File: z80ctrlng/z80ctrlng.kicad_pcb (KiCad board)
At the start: 2 copper layers, 99.8 x 49.9 mm, 54 parts, among them J1 BUS, J10 QWIIC, J11 CLOCK, J2 MICRO_SD, J3 UEXT, J4 SERIAL, J5 3V_LINK, J6 UPDI, J7 UEXT_CS, J8 S1_LINK, J9 S2_LINK, Q1 BSS138, SW1 RESET, SW2 BANK_EN, SW3 RTC, SW4 RTC, U1 AVR128DB64x-xPT, U2 MIC5504-3.3YM5, U3 MCP7940N-xST, U5 74HCT574, U6 74HCT257, U7 AS6C4008-55PCN, Y1 32kHz

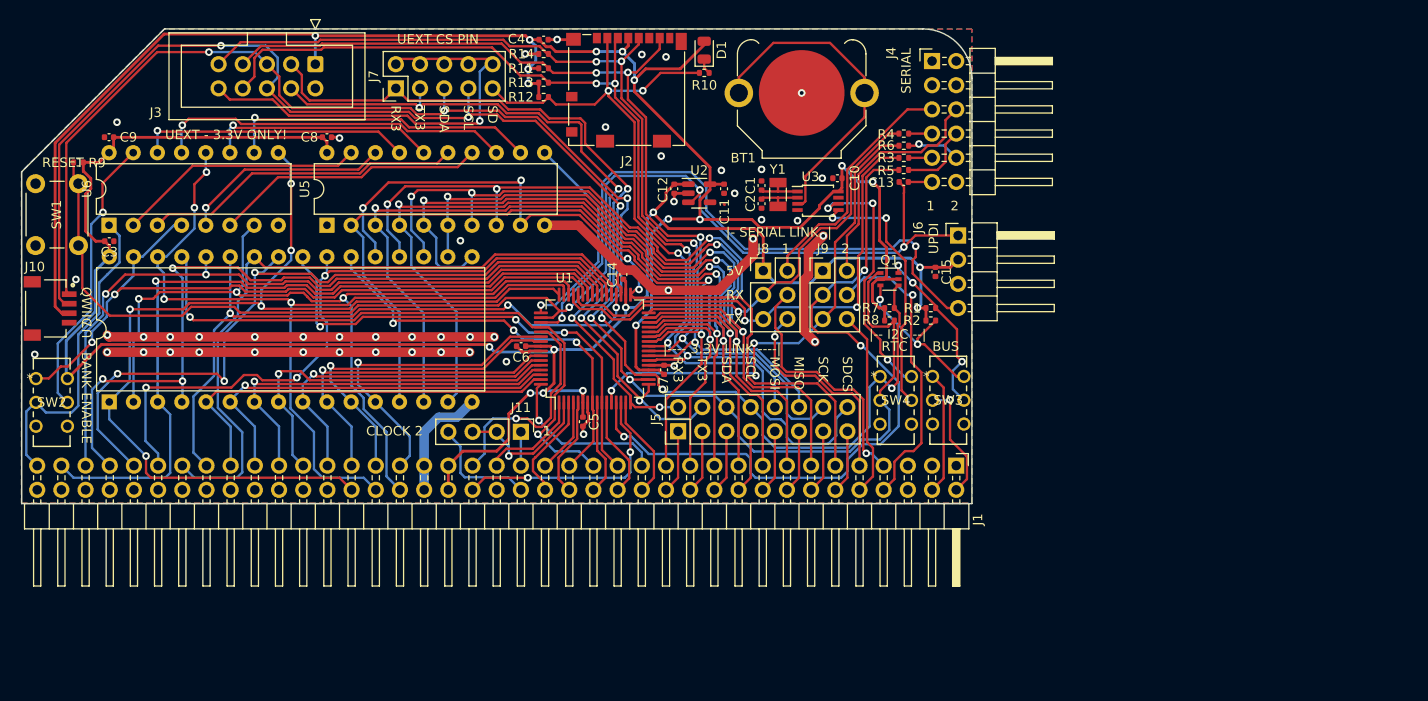
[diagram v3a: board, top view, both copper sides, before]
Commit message: Switch to RCBus-80 footprints, JLCPCB preferred components
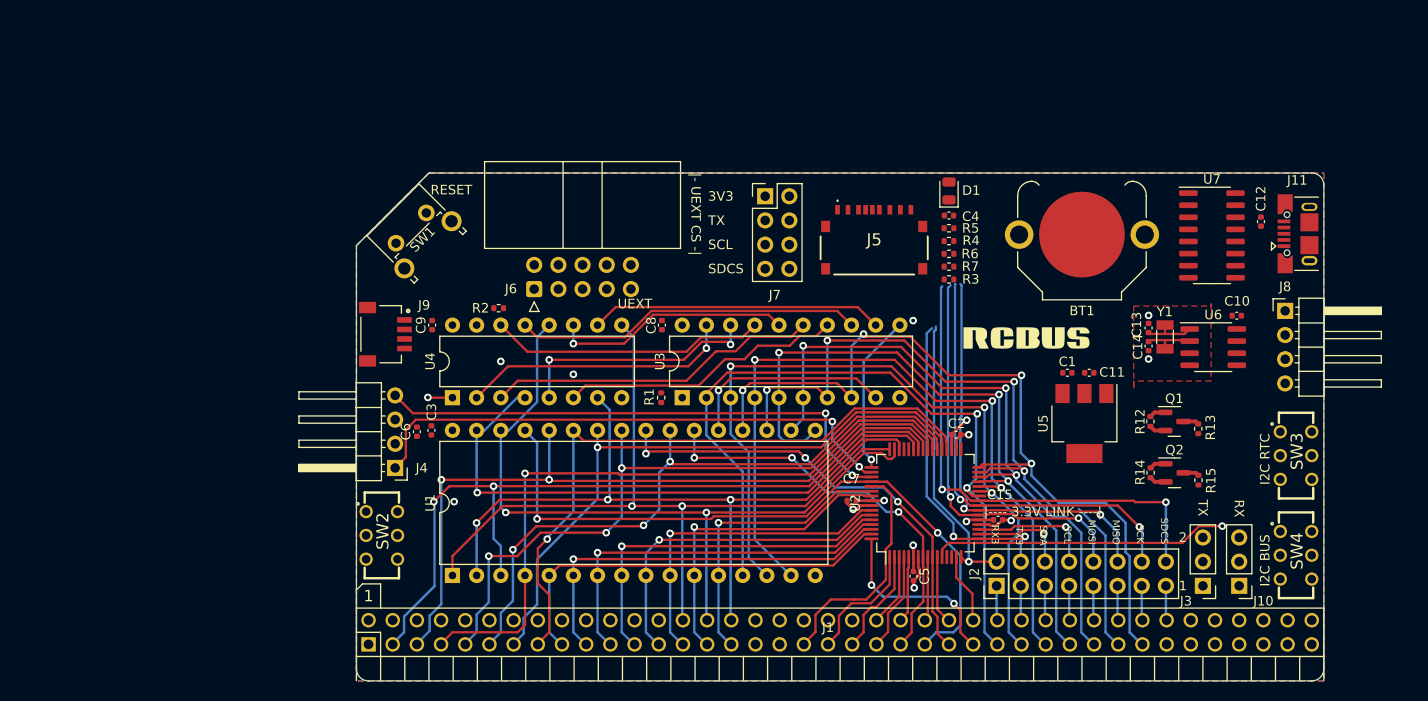
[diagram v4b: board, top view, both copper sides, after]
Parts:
- removed R10: 330, Resistor_SMD:R_0402_1005Metric
- removed R11: 100K, Resistor_SMD:R_0402_1005Metric
- removed R8: 4.7K, Resistor_SMD:R_0402_1005Metric
- removed R9: 1K, Resistor_SMD:R_0402_1005Metric
- added LOGO3: RCBUS_Logo, My_Components:RCBUS_Logo, F.Cu at (198.4, 90.7)
- added Q2: BSS138, Package_TO_SOT_SMD:SOT-23, F.Cu at (213.7, 104.9)
- added R15: 4.7K, Resistor_SMD:R_0402_1005Metric, F.Cu at (216.2, 105.7)
- added U4: 74HCT257, Package_DIP:DIP-16_W7.62mm, F.Cu at (137.8, 97.0)
- BT1: value Battery -> CR1216
- C1, C2: value 0.6pf -> 0.1uf
- C10, C9: value 0.1uf -> 1uf
- C11, C12: value 1uf -> 0.1uf
- C13, C14: value 0.1uf -> 0.6pf
- J1: value BUS -> RCBus-80; footprint Connector_PinHeader_2.54mm:PinHeader_2x39_P2.54mm_Horizontal -> Custom:RCBus-80
- J10: value QWIIC -> RX_LINK; footprint Custom:JST_SM04B-SRSS-TB_LF__SN_ -> Connector_PinHeader_2.54mm:PinHeader_1x03_P2.54mm_Vertical
- J11: value CLOCK -> USB_B_Micro; footprint Connector_PinHeader_2.54mm:PinHeader_1x04_P2.54mm_Vertical -> Connector_USB:USB_Micro-B_XKB_U254-051T-4BH83-F1S
- J2: value MICRO_SD -> 3V_LINK; footprint Connector_Card:microSD_HC_Molex_104031-0811 -> Connector_PinHeader_2.54mm:PinHeader_2x08_P2.54mm_Vertical
- J3: value UEXT -> TX_LINK; footprint Connector_IDC:IDC-Header_2x05_P2.54mm_Vertical -> Connector_PinHeader_2.54mm:PinHeader_1x03_P2.54mm_Vertical
- J4: value SERIAL -> UPDI; footprint Connector_PinHeader_2.54mm:PinHeader_2x06_P2.54mm_Horizontal -> Connector_PinHeader_2.54mm:PinHeader_1x04_P2.54mm_Horizontal
- J5: value 3V_LINK -> XKTF-0803-0; footprint Connector_PinHeader_2.54mm:PinHeader_2x08_P2.54mm_Vertical -> SamacSys_Parts:XKTF08030
- J6: value UPDI -> UEXT; footprint Connector_PinHeader_2.54mm:PinHeader_1x04_P2.54mm_Horizontal -> Connector_IDC:IDC-Header_2x05_P2.54mm_Horizontal
- J7: value UEXT_CS -> UXCS; footprint Connector_PinHeader_2.54mm:PinHeader_2x05_P2.54mm_Vertical -> Connector_PinHeader_2.54mm:PinHeader_2x04_P2.54mm_Vertical
- J8: value S1_LINK -> SERIAL; footprint Connector_PinHeader_2.54mm:PinHeader_2x03_P2.54mm_Vertical -> Connector_PinHeader_2.54mm:PinHeader_1x04_P2.54mm_Horizontal
- J9: value S2_LINK -> SM04B-SRSS-TB; footprint Connector_PinHeader_2.54mm:PinHeader_2x03_P2.54mm_Vertical -> Custom:JST_SM04B-SRSS-TB_LF__SN_
- Q1: footprint Package_TO_SOT_SMD:SOT-363_SC-70-6 -> Package_TO_SOT_SMD:SOT-23
- R1, R2: value 4.7K -> 10K
- R12, R13, R14: value 100K -> 4.7K
- R3, R4, R6: value 1K -> 100K
- R5: value 1K -> 100
- R7: value 4.7K -> 100K
- SW1: footprint Button_Switch_THT:SW_PUSH_6mm -> Button_Switch_THT:SW_Tactile_SPST_Angled_PTS645Vx31-2LFS
- SW2, SW3: footprint Custom:SWITCH_011CQN -> SamacSys_Parts:JS202011CQN
- SW4: value RTC -> BUS; footprint Custom:SWITCH_011CQN -> SamacSys_Parts:JS202011CQN
- U1: value AVR128DB64x-xPT -> AS6C4008-55PCN; footprint Package_QFP:TQFP-64_10x10mm_P0.5mm -> Package_DIP:DIP-32_W15.24mm
- U2: value MIC5504-3.3YM5 -> AVR128DB64T-I/PT; footprint Package_TO_SOT_SMD:SOT-23-5 -> Package_QFP:TQFP-64_10x10mm_P0.5mm
- U3: value MCP7940N-xST -> 74HCT574; footprint Package_SO:TSSOP-8_3x3mm_P0.65mm -> Package_DIP:DIP-20_W7.62mm
- U5: value 74HCT574 -> AMS1117-3.3; footprint Package_DIP:DIP-20_W7.62mm -> Package_TO_SOT_SMD:SOT-223-3_TabPin2
- U6: value 74HCT257 -> PCF8563T; footprint Package_DIP:DIP-16_W7.62mm -> Package_SO:SOIC-8_3.9x4.9mm_P1.27mm
- U7: value AS6C4008-55PCN -> CH340C; footprint Package_DIP:DIP-32_W15.24mm -> Package_SO:SOIC-16_3.9x9.9mm_P1.27mm
- moved J10 126.3 mm to (220.5, 116.8), turned to 180 degrees
- moved U7 117.1 mm to (217.6, 80.0), turned to 0 degrees
- moved U6 116.7 mm to (217.7, 91.7), turned to 0 degrees
- moved J3 108.1 mm to (216.7, 116.8), turned to 180 degrees
- moved J11 85.0 mm to (227.5, 79.8), turned to 90 degrees
- moved U5 82.2 mm to (204.2, 99.7), turned to -90 degrees
- moved R13 77.8 mm to (216.2, 100.3), turned to 90 degrees
- moved R14 77.5 mm to (211.2, 104.9), turned to -90 degrees
- moved R12 72.3 mm to (211.1, 99.5), turned to -90 degrees
- moved J4 70.8 mm to (131.8, 104.4), turned to 180 degrees
- moved J2 65.0 mm to (195.0, 116.8), turned to 90 degrees
- moved C12 61.7 mm to (222.8, 78.5), turned to 90 degrees
- moved C14 55.7 mm to (211.0, 91.6), turned to -90 degrees
- moved J8 55.0 mm to (225.3, 87.9)
- moved SW4 47.5 mm to (226.4, 113.6), turned to -90 degrees
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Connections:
- BT1 pad 1: Net-(BT1-+) -> +3.3V
- C1 pad 1: Net-(U3-X1) -> +5V
- C12 pad 1: +5V -> Net-(U7-~{DTR})
- C12 pad 2: GND -> ~{RESET}
- C13 pad 1: Net-(J4-Pin_11) -> Net-(U6-OSCI)
- C13 pad 2: /~{RESET} -> GND
- C14 pad 1: +5V -> Net-(U6-OSCO)
- C15 pad 1: +5V -> +3.3V
- C2 pad 1: Net-(U3-X2) -> +5V
- C7 pad 1: +3.3V -> +5V
- J1 pad 1: /USER3 -> /A15
- J1 pad 10: /BTX2 -> /A6
- J1 pad 11: /D7 -> /A5
- J1 pad 12: /D15 -> /A4
- J1 pad 13: /D6 -> /A3
- J1 pad 14: /D14 -> /A2
- J1 pad 15: /D5 -> /A1
- J1 pad 16: /D13 -> /A0
- J1 pad 17: /D4 -> GND
- J1 pad 18: /D12 -> +5V
- J1 pad 19: /D3 -> /~{M1}
- J1 pad 2: /USER7 -> /A14
- J1 pad 20: /D11 -> /~{Z80RST}
- J1 pad 21: /D2 -> /Z80CLK
- J1 pad 22: /D10 -> /~{INT}
- J1 pad 23: /D1 -> /~{MREQ}
- J1 pad 24: /D9 -> /~{WR}
- J1 pad 25: /D0 -> /~{RD}
- J1 pad 26: /D8 -> /~{IORQ}
- J1 pad 27: /~{IORQ} -> /D0
- J1 pad 28: /~{NMI} -> /D1
- J1 pad 29: /~{RD} -> /D2
- J1 pad 3: /USER2 -> /A13
- J1 pad 30: /~{WAIT} -> /D3
- J1 pad 31: /~{WR} -> /D4
- J1 pad 32: /~{BUSRQ} -> /D5
- J1 pad 33: /~{MREQ} -> /D6
- J1 pad 34: /~{HALT} -> /D7
- J1 pad 35: /~{INT} -> /BTX1
- J1 pad 36: /~{BUSACK} -> /BRX1
- J1 pad 37: /CLOCK1 -> /USER1
- J1 pad 38: /CLOCK2 -> /USER2
- J1 pad 39: /~{Z80RST} -> /USER3
- J1 pad 4: /USER6 -> /A12
- J1 pad 40: /PAGE -> unconnected-(J1-Pin_40-Pad40)
- J1 pad 41: /~{M1} -> /p41
- J1 pad 42: /~{RFSH} -> /p42
- J1 pad 43: +5V -> /p43
- J1 pad 44: +5V -> /p44
- J1 pad 45: GND -> /p45
- J1 pad 46: GND -> /p46
- J1 pad 47: /A0 -> /p47
- J1 pad 48: /A16 -> /p48
- J1 pad 49: /A1 -> /A23
- J1 pad 5: /USER1 -> /A11
- J1 pad 50: /A17 -> /A22
- J1 pad 51: /A2 -> /A21
- J1 pad 52: /A18 -> /A20
- J1 pad 53: /A3 -> /A19
- J1 pad 54: /A19 -> /A18
- J1 pad 55: /A4 -> /A17
- J1 pad 56: /A20 -> /A16
- J1 pad 57: /A5 -> GND
- J1 pad 58: /A21 -> +5V
- J1 pad 59: /A6 -> /~{RFSH}
- J1 pad 6: /USER5 -> /A10
- J1 pad 60: /A22 -> /PAGE
- J1 pad 61: /A7 -> /CLOCK2
- J1 pad 62: /A23 -> /~{BUSACK}
- J1 pad 63: /A8 -> /~{HALT}
- J1 pad 64: /p48 -> /~{BUSRQ}
- J1 pad 65: /A9 -> /~{WAIT}
- J1 pad 66: /p47 -> /~{NMI}
- J1 pad 67: /A10 -> /D8
- J1 pad 68: /p46 -> /D9
- J1 pad 69: /A11 -> /D10
- J1 pad 7: /BRX -> /A9
- J1 pad 70: /p45 -> /D11
- J1 pad 71: /A12 -> /D12
- J1 pad 72: /p44 -> /D13
- J1 pad 73: /A13 -> /D14
- J1 pad 74: /p43 -> /D15
- J1 pad 75: /A14 -> /BTX2
- J1 pad 76: /p42 -> /BRX2
- J1 pad 77: /A15B -> /USER5
- J1 pad 78: /p41 -> SCL5V
- J1 pad 8: /BRX2 -> /A8
- J1 pad 9: /BTX -> /A7
- J10 pad 1: /SCL -> /BRX1
- J10 pad 2: /SDA -> RX2
- J10 pad 3: +3.3V -> /BRX2
- J11 pad 1: /CLOCK1 -> unconnected-(J11-VBUS-Pad1)
- J11 pad 2: /Z80CLK -> unconnected-(J11-D--Pad2)
- J11 pad 3: /Z80CLK -> unconnected-(J11-D+-Pad3)
- J11 pad 4: /CLOCK2 -> unconnected-(J11-ID-Pad4)
- J2 pad 1: unconnected-(J2-DAT2-Pad1) -> /D8
- J2 pad 10: unconnected-(J2-DET_A-Pad10) -> MOSI
- J2 pad 11: GND -> /D13
- J2 pad 2: /~{SDCS} -> RX3
- J2 pad 3: /MOSI -> /D9
- J2 pad 4: +3.3V -> TX3
- J2 pad 5: /SCK -> /D10
- J2 pad 6: GND -> SDA
- J2 pad 7: /MISO -> /D11
- J2 pad 8: unconnected-(J2-DAT1-Pad8) -> SCL
- J2 pad 9: unconnected-(J2-DET_B-Pad9) -> /D12
- J3 pad 1: +3.3V -> /BTX1
- J3 pad 2: GND -> TX2
- J3 pad 3: /TX3 -> /BTX2
- J4 pad 1: GND -> ~{RESET}
- J4 pad 2: GND -> +5V
- J4 pad 3: unconnected-(J4-Pin_3-Pad3) -> GND
- J4 pad 4: unconnected-(J4-Pin_4-Pad4) -> UPDI
- J6 pad 1: /~{RESET} -> +3.3V
- J6 pad 2: +5V -> GND
- J6 pad 3: GND -> TX3
- J6 pad 4: /UPDI -> RX3
- J7 pad 1: /TX3 -> +3.3V
- J7 pad 2: /~{UXCS} -> Net-(J6-Pin_10)
- J7 pad 3: /RX3 -> TX3
- J7 pad 4: /~{UXCS} -> Net-(J6-Pin_10)
- J7 pad 5: /SCL -> SCL
- J7 pad 6: /~{UXCS} -> Net-(J6-Pin_10)
- J7 pad 7: /SDA -> ~{SDCS}
- J7 pad 8: /~{UXCS} -> Net-(J6-Pin_10)
- J8 pad 2: /5VS1 -> RX2
- J8 pad 3: /RX -> TX2
- J8 pad 4: /BRX -> GND
- J9 pad 1: +5V -> SCL
- J9 pad 2: /5VS2 -> SDA
- J9 pad 3: /RX2 -> +3.3V
- J9 pad 4: /BRX2 -> GND
- Q1 pad 1: /SDA -> +3.3V
- Q1 pad 2: +3.3V -> Net-(Q1-S)
- Q1 pad 3: /SCL5V -> Net-(Q1-D)
- R1 pad 1: +5V -> /~{MREQ}
- R1 pad 2: /SDA5V -> +5V
- R12 pad 2: /~{SDCS} -> Net-(Q1-S)
- R13 pad 1: +3.3V -> +5V
- R13 pad 2: /MOSI -> Net-(Q1-D)
- R14 pad 1: GND -> +3.3V
- R14 pad 2: /SCK -> Net-(Q2-S)
- R2 pad 1: +5V -> ~{RESET}
- R2 pad 2: /SCL5V -> +5V
- R3 pad 1: Net-(J4-Pin_9) -> Net-(R3-Pad1)
- R3 pad 2: /TX -> MISO
- R4 pad 1: Net-(J4-Pin_7) -> Net-(R3-Pad1)
- R4 pad 2: /RX -> ~{SDCS}
- R5 pad 1: /RX2 -> ~{SDCS}
- R5 pad 2: Net-(J4-Pin_8) -> Net-(D1-K)
- R6 pad 1: Net-(J4-Pin_10) -> Net-(R3-Pad1)
- R6 pad 2: /TX2 -> MOSI
- R7 pad 1: +3.3V -> GND
- R7 pad 2: /SCL -> SCK
- SW1 pad 2: /~{RESET} -> ~{RESET}
- SW2 pad 2: /A15B -> /A15
- SW3 pad 1: /USER6 -> Net-(Q2-S)
- SW3 pad 2: /USER7 -> SDA
- SW3 pad 4: unconnected-(SW3-Pad4) -> Net-(Q1-S)
- SW3 pad 5: /SDA5V -> SCL
- SW3 pad 6: /SCL5V -> unconnected-(SW3-Pad6)
- SW4 pad 1: /SCL -> Net-(Q2-D)
- SW4 pad 2: /SDA -> SCL5V
- SW4 pad 4: unconnected-(SW4-Pad4) -> Net-(Q1-D)
- SW4 pad 5: Net-(U3-SDA) -> SDA5V
- SW4 pad 6: Net-(U3-SCL) -> unconnected-(SW4-Pad6)
- U1 pad 1: /~{Z80RST} -> /A18
- U1 pad 10: /~{RD} -> /A2
- U1 pad 11: /~{WAIT} -> /A1
- U1 pad 12: /TX2 -> /A0
- U1 pad 13: /RX2 -> /D0
- U1 pad 14: /~{RFSH} -> /D1
- U1 pad 15: /~{NMI} -> /D2
- U1 pad 16: /RX3 -> GND
- U1 pad 17: /TX3 -> /D3
- U1 pad 18: /SDA -> /D4
- U1 pad 19: /SCL -> /D5
- U1 pad 2: /Z80CLK -> /A16
- U1 pad 20: +3.3V -> /D6
- U1 pad 21: GND -> /D7
- U1 pad 22: /MOSI -> /~{MREQ}
- U1 pad 23: /MISO -> /A10
- U1 pad 24: /SCK -> /~{RD}
- U1 pad 25: /~{SDCS} -> /A11
- U1 pad 26: /D0 -> /A9
- U1 pad 27: /D1 -> /A8
- U1 pad 28: /D2 -> /A13
- U1 pad 29: /D3 -> /~{WR}
- U1 pad 3: /~{BUSACK} -> /A14
- U1 pad 30: /D4 -> /A17
- U1 pad 31: /D5 -> /A15
- U1 pad 32: /D6 -> +5V
- U1 pad 4: /~{INT} -> /A12
- U1 pad 5: /~{HALT} -> /A7
- U1 pad 6: +5V -> /A6
- U1 pad 7: GND -> /A5
- U1 pad 8: /~{MREQ} -> /A4
- U1 pad 9: /~{BUSRQ} -> /A3
- U2 pad 1: +5V -> /~{Z80RST}
- U2 pad 2: GND -> /Z80CLK
- U2 pad 3: /~{RESET} -> /~{BUSACK}
- U2 pad 4: unconnected-(U2-NC-Pad4) -> /~{INT}
- U2 pad 5: +3.3V -> /~{HALT}
- U3 pad 1: Net-(U3-X1) -> GND
- U3 pad 2: Net-(U3-X2) -> /D0
- U3 pad 3: Net-(BT1-+) -> /D1
- U3 pad 4: GND -> /D2
- U3 pad 5: Net-(U3-SDA) -> /D3
- U3 pad 6: Net-(U3-SCL) -> /D4
- U3 pad 7: unconnected-(U3-MFP-Pad7) -> /D5
- U3 pad 8: +3.3V -> /D6
- U5 pad 2: /D0 -> +3.3V
- U5 pad 3: /D1 -> +5V
- U6 pad 1: /A15B -> Net-(U6-OSCI)
- U6 pad 2: /BA15 -> Net-(U6-OSCO)
- U6 pad 3: /BB15 -> unconnected-(U6-~{INT}-Pad3)
- U6 pad 4: /A15 -> GND
- U6 pad 5: /BA16 -> Net-(Q1-S)
- U6 pad 6: /BB16 -> Net-(Q2-S)
- U6 pad 7: /A16 -> unconnected-(U6-CLKO-Pad7)
- U6 pad 8: GND -> +3.3V
- U7 pad 1: /A18 -> unconnected-(U7-GND-Pad1)
- U7 pad 10: /A2 -> unconnected-(U7-~{DSR}-Pad10)
- U7 pad 11: /A1 -> unconnected-(U7-~{RI}-Pad11)
- U7 pad 12: /A0 -> unconnected-(U7-~{DCD}-Pad12)
- U7 pad 13: /D0 -> Net-(U7-~{DTR})
- U7 pad 14: /D1 -> unconnected-(U7-~{RTS}-Pad14)
- U7 pad 15: /D2 -> unconnected-(U7-R232-Pad15)
- U7 pad 16: GND -> unconnected-(U7-VCC-Pad16)
- U7 pad 2: /A16 -> unconnected-(U7-TXD-Pad2)
- U7 pad 3: /A14 -> unconnected-(U7-RXD-Pad3)
- U7 pad 4: /A12 -> unconnected-(U7-V3-Pad4)
- U7 pad 5: /A7 -> unconnected-(U7-UD+-Pad5)
- U7 pad 6: /A6 -> unconnected-(U7-UD--Pad6)
- U7 pad 7: /A5 -> unconnected-(U7-NC-Pad7)
- U7 pad 8: /A4 -> unconnected-(U7-NC-Pad8)
- U7 pad 9: /A3 -> unconnected-(U7-~{CTS}-Pad9)
- Y1 pad 1: Net-(U3-X2) -> Net-(U6-OSCO)
- Y1 pad 2: Net-(U3-X1) -> Net-(U6-OSCI)
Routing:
- net +5V: track 218.1 -> 8.29 mm, vias 9 -> 4
- net +3.3V: track 196.8 -> 7.19 mm, vias 12 -> 1
- net /SDA: track 172.2 -> 0.00 mm, vias 5 -> 0
- net /SCL: track 159.9 -> 0.00 mm, vias 6 -> 0
- net GND: track 150.9 -> 13.6 mm, vias 49 -> 8
- net /~{RESET}: track 137.0 -> 0.00 mm, vias 3 -> 0
- net /SCK: track 106.7 -> 0.00 mm, vias 4 -> 0
- net /MISO: track 102.0 -> 0.00 mm, vias 4 -> 0
- net /MOSI: track 99.9 -> 0.00 mm, vias 4 -> 0
- net /~{SDCS}: track 92.5 -> 0.00 mm, vias 4 -> 0
- net /TX3: track 81.2 -> 0.00 mm, vias 3 -> 0
- net /RX2: track 77.5 -> 0.00 mm, vias 3 -> 0
- net /RX3: track 75.7 -> 0.00 mm, vias 4 -> 0
- net /UPDI: track 66.4 -> 0.00 mm, vias 2 -> 0
- net /D7: track 84.4 -> 22.1 mm, vias 4 -> 1
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- added copper zone on F.Cu, net +5V
- added copper zone on In2.Cu, net +5V
- added copper zone on In1.Cu, net GND
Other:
- board size 99.8 x 49.9 mm -> 101.6 x 53.3 mm
- copper layers 2 -> 4
- board text added: "I2C BUS"
- board text added: "I2C RTC"
- board text added: "PA5 PA6"
- board text added: "PA7 PB0"
- board text added: "PB1 PG0"
- board text added: "PB3 PB2"
- board text added: "PB7 PA2"
- board text added: "UEXT"
- board text added: "|- UEXT CS -|"
- board text removed: "BANK ENABLE"
- board text removed: "BUS"
- board text removed: "CLOCK 2"
- board text removed: "PA2"
- board text removed: "PA5^"
- board text removed: "PA6"
- board text removed: "PA7^"
- board text removed: "PB1^"
- board text removed: "PB3^"
- board text removed: "PB4^"
- board text removed: "PB5^"
- board text removed: "PB6^"
- board text removed: "PB7^"
- board text removed: "PF0^"
- board text removed: "PF1^"
- board text removed: "PF2^"
- board text removed: "PF3^"
- board text removed: "PF4^"
- board text removed: "QWIIC"
- board text removed: "RTC"
- board text removed: "SD"
- board text removed: "SERIAL"
- board text removed: "UEXT - 3.3V ONLY!"
- board text removed: "UEXT CS PIN"
- board text removed: "UPDI"
- board text removed: "|- SERIAL LINK -|"
- board text removed: "|-- I2C --|"

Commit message: Final touches... I hope
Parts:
- removed J8: SERIAL, Connector_PinHeader_2.54mm:PinHeader_1x04_P2.54mm_Horizontal
- added C16: 0.1uf, Capacitor_SMD:C_0402_1005Metric, F.Cu at (220.3, 75.3)
- added D2: 1N5819WS, Diode_SMD:D_SOD-323_HandSoldering, F.Cu at (216.5, 88.9)
- added D3: 1N5819WS, Diode_SMD:D_SOD-323_HandSoldering, F.Cu at (211.8, 88.8)
- added H1: MountingHole, MountingHole:MountingHole_3.2mm_M3, F.Cu at (132.8, 91.2)
- added R8: 1K, Resistor_SMD:R_0402_1005Metric, F.Cu at (212.8, 85.8)
- C10, C9: footprint Capacitor_SMD:C_0402_1005Metric -> Capacitor_SMD:C_1206_3216Metric
- J11: value USB_B_Micro -> U254-051T-4BH81-S2S; footprint Connector_USB:USB_Micro-B_XKB_U254-051T-4BH83-F1S -> SamacSys_Parts:U254051T4BH81S2S
- J4: value UPDI -> DEBUG; footprint Connector_PinHeader_2.54mm:PinHeader_1x04_P2.54mm_Horizontal -> Connector_PinHeader_2.54mm:PinHeader_2x04_P2.54mm_Horizontal
- U2: value AVR128DB64T-I/PT -> AVR128DB64x-xPT
- moved J4 95.2 mm to (225.6, 87.6), turned to 0 degrees
- moved C6 89.6 mm to (223.2, 91.5), turned to -90 degrees
- moved C9 68.6 mm to (203.1, 101.9), turned to -90 degrees
- moved C1 64.8 mm to (137.9, 87.8), turned to 180 degrees
- moved C15 31.4 mm to (220.2, 90.9)
- moved C11 20.3 mm to (193.0, 111.0), turned to 90 degrees
- moved C10 15.3 mm to (212.9, 101.9), turned to 90 degrees
- moved J9 10.4 mm to (132.8, 100.8)
- moved C12 9.14 mm to (223.2, 87.6), turned to -90 degrees
- moved C4 8.24 mm to (182.2, 75.2), turned to 180 degrees
- moved Q1 4.95 mm to (218.4, 101.0)
- moved R12 4.95 mm to (215.9, 101.0)
- moved R14 4.84 mm to (215.9, 106.0)
- moved Q2 4.81 mm to (218.4, 105.8)
- moved U5 4.37 mm to (208.0, 101.9)
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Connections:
- net /BRX1 renamed /RX1B
- net /BRX2 renamed /RX2B
- net /BTX1 renamed /TX1B
- net /BTX2 renamed /TX2B
- net ~{SDCS} renamed ~{SS}
- BT1 pad 1: +3.3V -> Net-(BT1-+)
- C15 pad 1: +3.3V -> Net-(D2-K)
- J1 pad 1: /A15 -> /A15B
- J10 pad 2: RX2 -> RXB
- J11 pad 2: unconnected-(J11-D--Pad2) -> Net-(J11-D-)
- J11 pad 3: unconnected-(J11-D+-Pad3) -> Net-(J11-D+)
- J11 pad 5: unconnected-(J11-GND-Pad5) -> GND
- J2 pad 2: RX3 -> TX3V
- J2 pad 4: TX3 -> RX3V
- J3 pad 2: TX2 -> TXB
- J4 pad 2: +5V -> TXB
- J4 pad 3: GND -> +5V
- J4 pad 4: UPDI -> +5V
- J5 pad MP1: GND -> unconnected-(J5-PadMP1)
- J5 pad MP2: GND -> unconnected-(J5-PadMP2)
- J5 pad MP3: GND -> unconnected-(J5-PadMP3)
- J5 pad MP4: GND -> unconnected-(J5-PadMP4)
- J6 pad 3: TX3 -> TX3V
- J6 pad 4: RX3 -> RX3V
- J7 pad 3: TX3 -> TX3V
- R3 pad 1: Net-(R3-Pad1) -> +3.3V
- R4 pad 1: Net-(R3-Pad1) -> +3.3V
- R6 pad 1: Net-(R3-Pad1) -> +3.3V
- SW2 pad 2: /A15 -> /A15B
- U2 pad 12: TX2 -> TXB
- U2 pad 13: RX2 -> RXB
- U2 pad 14: /~{RFSH} -> /BCK
- U2 pad 16: RX3 -> TX3V
- U2 pad 17: TX3 -> RX3V
- U2 pad 44: TX1 -> TXU
- U2 pad 45: RX1 -> RXU
- U2 pad 46: /A16 -> CTS
- U2 pad 47: /A17 -> /A16
- U2 pad 48: /A18 -> /A17
- U2 pad 49: /BCK -> /A18
- U4 pad 1: /A15 -> /A15B
- U6 pad 8: +3.3V -> Net-(D2-K)
- U7 pad 1: unconnected-(U7-GND-Pad1) -> GND
- U7 pad 16: unconnected-(U7-VCC-Pad16) -> +5V
- U7 pad 2: unconnected-(U7-TXD-Pad2) -> TXU
- U7 pad 3: unconnected-(U7-RXD-Pad3) -> RXU
- U7 pad 5: unconnected-(U7-UD+-Pad5) -> Net-(J11-D-)
- U7 pad 6: unconnected-(U7-UD--Pad6) -> Net-(J11-D+)
- U7 pad 9: unconnected-(U7-~{CTS}-Pad9) -> CTS
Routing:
- net SCL: track 13.1 -> 158.6 mm, vias 1 -> 5
- net SDA: track 10.1 -> 154.5 mm, vias 1 -> 4
- net ~{RESET}: track 57.2 -> 183.5 mm
- net TX3V: track 0.00 -> 95.9 mm, vias 0 -> 3
- net RX3V: track 0.00 -> 88.0 mm, vias 0 -> 1
- net TXB: track 0.00 -> 66.8 mm
- net RXB: track 0.00 -> 62.3 mm
- net /D7: track 22.1 -> 81.5 mm
- net MISO: track 44.4 -> 101.4 mm, vias 2 -> 3
- net CTS: track 0.00 -> 51.0 mm, vias 0 -> 2
- net RXU: track 0.00 -> 48.5 mm, vias 0 -> 2
- net TXU: track 0.00 -> 48.3 mm, vias 0 -> 2
- net MOSI: track 42.8 -> 89.7 mm, vias 2 -> 3
- net SCK: track 46.7 -> 92.4 mm, vias 2 -> 3
- net ~{SS}: track 51.7 -> 94.5 mm, vias 2 -> 3
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- added copper zone on F.Cu, net +3.3V
- added copper zone on In2.Cu, net +3.3V
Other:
- board text added: "BANK EN"
- board text added: "QWIIC"
- board text added: "|-UEXT CS-|"
- board text added: "~{SS}"
- board text removed: "5V"
- board text removed: "GND"
- board text removed: "PA0"
- board text removed: "PA1"
- board text removed: "PA3"
- board text removed: "PA4"
- board text removed: "PA5 PA6"
- board text removed: "PA7 PB0"
- board text removed: "PB0"
- board text removed: "PB1 PG0"
- board text removed: "PB2"
- board text removed: "PB3 PB2"
- board text removed: "PB7 PA2"
- board text removed: "PC0"
- board text removed: "PC1"
- board text removed: "PC2"
- board text removed: "PC3"
- board text removed: "PC4"
- board text removed: "PC5"
- board text removed: "PC6"
- board text removed: "PC7"
- board text removed: "PD0"
- board text removed: "PD1"
- board text removed: "PD2"
- board text removed: "PD3"
- board text removed: "PD4"
- board text removed: "PD5"
- board text removed: "PD6"
- board text removed: "PD7"
- board text removed: "PE0"
- board text removed: "PE1"
- board text removed: "PE2"
- board text removed: "PE3"
- board text removed: "PE4"
- board text removed: "PE5"
- board text removed: "PE6"
- board text removed: "PE7"
- board text removed: "PF2"
- board text removed: "PF3"
- board text removed: "PF4"
- board text removed: "PF5"
- board text removed: "PG0"
- board text removed: "PG1"
- board text removed: "PG2"
- board text removed: "PG3"
- board text removed: "PG4"
- board text removed: "PG5"
- board text removed: "PG6"
- board text removed: "PG7"
- board text removed: "RX3"
- board text removed: "SDCS"
- board text removed: "TX3"
- board text removed: "|- UEXT CS -|"

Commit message: Fixing mistakes on RX/TX, better isolation for RTC
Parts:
- removed C14: 0.6pf, Capacitor_SMD:C_0402_1005Metric
- added NT1: NetTie_2, NetTie:NetTie-2_SMD_Pad0.5mm, F.Cu at (216.9, 96.3)
- C13: value 0.6pf -> 27pf; footprint Capacitor_SMD:C_0402_1005Metric -> Capacitor_SMD:C_0603_1608Metric
- moved D3 7.57 mm to (219.4, 88.9)
- moved C13 5.15 mm to (216.0, 91.4), turned to 180 degrees
- moved D2 2.99 mm to (213.5, 88.8)
- moved R8 1.73 mm to (211.1, 85.8)
- moved C15 0.66 mm to (220.2, 91.6)
- moved U6 0.66 mm to (217.7, 94.9)
- moved C10 0.64 mm to (212.9, 102.5)
- moved C9 0.64 mm to (203.1, 102.5)
- moved U5 0.64 mm to (208.0, 102.5)
- moved Y1 0.46 mm to (212.7, 93.6)
- moved C6 0.41 mm to (222.8, 91.4)
- moved J4 0.41 mm to (225.1, 87.6)
- moved C12 0.41 mm to (222.8, 87.6)
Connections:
- net UPDI renamed Net-(J4-Pin_7)
- C13 pad 1: Net-(U6-OSCI) -> GND1
- C13 pad 2: GND -> Net-(U6-OSCI)
- J4 pad 2: TXB -> RXB
- J4 pad 8: RXB -> TXB
- J5 pad G1: unconnected-(J5-DET-PadG1) -> GND
- U2 pad 10: /~{RD} -> /Z80CLK
- U2 pad 2: /Z80CLK -> /~{RD}
- U7 pad 2: TXU -> RXU
- U7 pad 3: RXU -> TXU
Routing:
- net GND1: track 0.00 -> 21.0 mm, vias 0 -> 2
- net GND: track 47.7 -> 30.5 mm, vias 34 -> 19
- net /Z80CLK: track 9.38 -> 18.9 mm
- net RXB: track 62.3 -> 71.7 mm
- net TXB: track 66.8 -> 59.6 mm
- net +3.3V: track 13.7 -> 20.1 mm, vias 17 -> 10
- net /~{RD}: track 59.0 -> 53.1 mm, vias 2 -> 3
- net /D7: track 81.5 -> 76.3 mm
- net Net-(U6-OSCO): track 5.23 -> 2.84 mm
- net ~{SS}: track 94.5 -> 92.4 mm
- net TXU: track 48.3 -> 46.7 mm
- net /A12: track 72.1 -> 73.7 mm
- net Net-(BT1-+): track 25.2 -> 24.0 mm
- net /D6: track 78.1 -> 76.9 mm
- net RXU: track 48.5 -> 49.5 mm
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- added copper zone on In1.Cu, net GND1
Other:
- board text added: "5V"
- board text added: "GND"
- board text added: "RST"
- board text added: "UPDI"
